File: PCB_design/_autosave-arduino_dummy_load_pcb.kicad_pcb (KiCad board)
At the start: 2 copper layers, 209.6 x 109.2 mm, 114 parts, among them J1 Barrel_Jack, J2 Conn_02x08_Odd_Even, U1 MCP3208

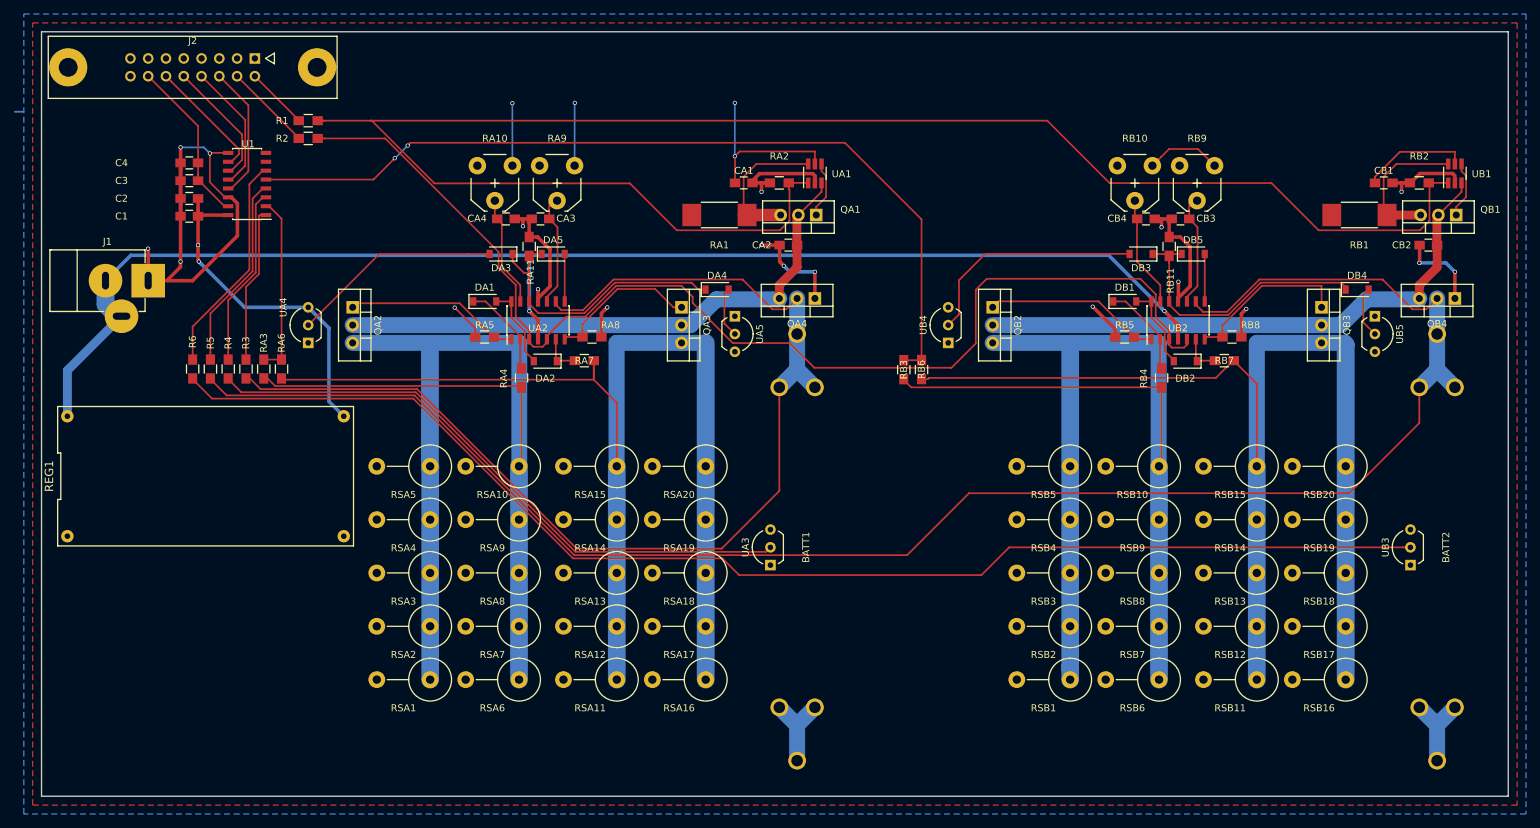
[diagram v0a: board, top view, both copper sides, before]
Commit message: Resized vias in order to reduce potential showstoppers in DFM Checks
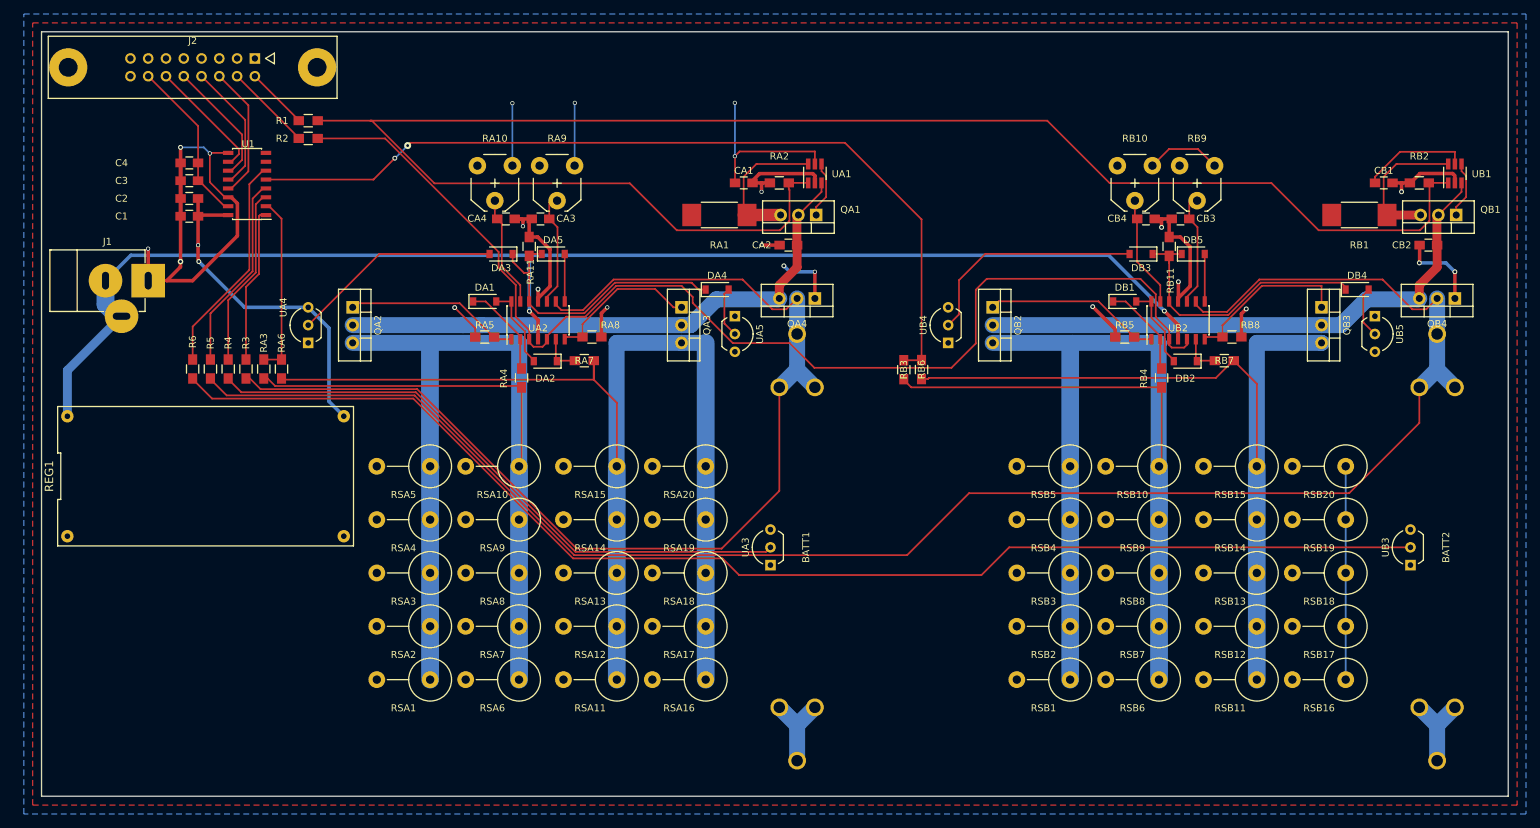
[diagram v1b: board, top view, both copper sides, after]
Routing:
- net Net-(QB3-Pad3): track 232.2 -> 180.8 mm
- net +9V: track 209.3 -> 197.8 mm
- net GND: track 205.9 -> 202.4 mm
- net (no net): track 1.27 -> 0.00 mm
- net CHARGE: track 250.5 -> 249.5 mm
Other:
- net class Default: via_dia 0.6 -> 0.7
